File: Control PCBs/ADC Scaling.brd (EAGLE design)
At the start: 50 x 50 mm, 25 parts, among them K1 G5V-2, K2 G5V-2, K3 G5V-2, K4 G5V-2

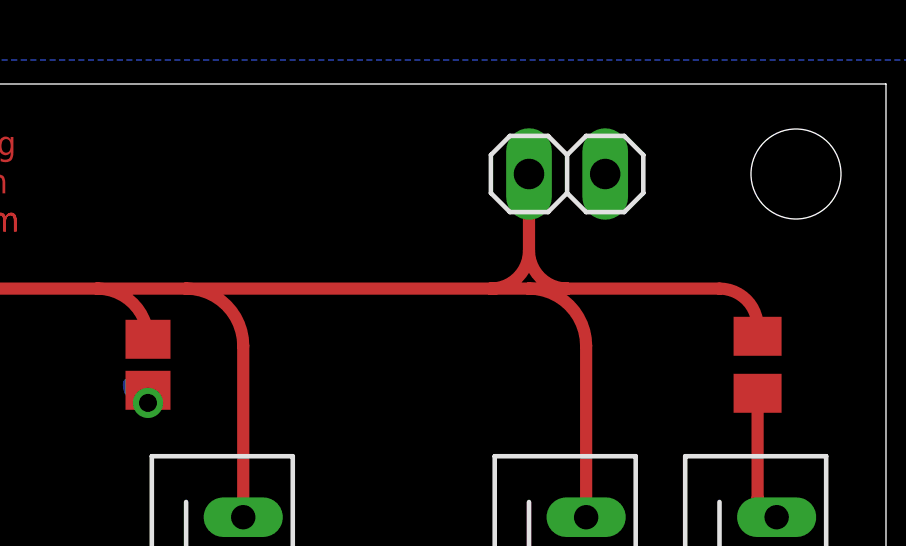
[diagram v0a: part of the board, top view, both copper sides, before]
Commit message: +Flip out connector on scaling pcb to aid in routing the adc +Routed ADC part of ADC/DAC board
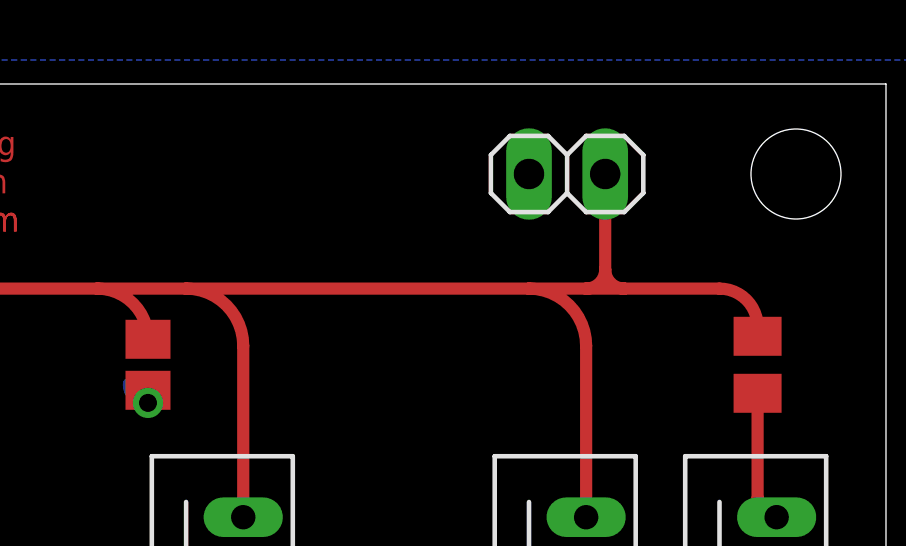
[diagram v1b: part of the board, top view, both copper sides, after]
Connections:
- net GND: now also JP2.1; no longer JP2.2
- net N$21: now also JP2.2; no longer JP2.1
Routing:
- net N$21: track 82.8 -> 81.6 mm
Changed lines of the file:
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@@
 <contactref element="R3" pad="S"/>
 <contactref element="R3" pad="A"/>
-<contactref element="JP2" pad="2"/>
 <contactref element="K1" pad="13"/>
 <contactref element="K1" pad="4"/>
@@
 <wire x1="7.62" y1="39.155" x2="5.295" y2="39.155" width="0.4064" layer="1"/>
 <wire x1="5.295" y1="39.155" x2="3.81" y2="40.64" width="0.4064" layer="1" curve="-90"/>
+<contactref element="JP2" pad="1"/>
 </signal>
 <signal name="N$1">
@@
 </signal>
 <signal name="N$21">
-<contactref element="JP2" pad="1"/>
 <contactref element="R7" pad="E"/>
 <contactref element="R4" pad="E"/>
@@
 <wire x1="15.24" y1="43.18" x2="23.71" y2="43.18" width="0.4064" layer="1"/>
 <wire x1="23.71" y1="43.18" x2="26.67" y2="43.18" width="0.4064" layer="1"/>
-<wire x1="26.67" y1="43.18" x2="36.83" y2="43.18" width="0.4064" layer="1"/>
-<wire x1="36.83" y1="43.18" x2="38.1" y2="43.18" width="0.4064" layer="1"/>
-<wire x1="38.1" y1="43.18" x2="39.37" y2="43.18" width="0.4064" layer="1"/>
-<wire x1="39.37" y1="43.18" x2="44.45" y2="43.18" width="0.4064" layer="1"/>
+<wire x1="26.67" y1="43.18" x2="38.1" y2="43.18" width="0.4064" layer="1"/>
+<wire x1="38.1" y1="43.18" x2="40.005" y2="43.18" width="0.4064" layer="1"/>
+<wire x1="40.005" y1="43.18" x2="41.275" y2="43.18" width="0.4064" layer="1"/>
+<wire x1="41.275" y1="43.18" x2="44.45" y2="43.18" width="0.4064" layer="1"/>
 <wire x1="44.45" y1="43.18" x2="45.72" y2="41.91" width="0.4064" layer="1" curve="-90"/>
 <wire x1="45.72" y1="41.91" x2="45.72" y2="41.59" width="0.4064" layer="1"/>
@@
 <contactref element="C1" pad="1"/>
 <wire x1="25.4" y1="41.49" x2="23.71" y2="43.18" width="0.4064" layer="1" curve="90"/>
-<wire x1="38.1" y1="44.45" x2="36.83" y2="43.18" width="0.4064" layer="1" curve="-90"/>
-<wire x1="38.1" y1="47" x2="38.1" y2="44.45" width="0.4064" layer="1"/>
-<wire x1="38.1" y1="44.45" x2="39.37" y2="43.18" width="0.4064" layer="1" curve="90"/>
+<contactref element="JP2" pad="2"/>
+<wire x1="40.64" y1="43.815" x2="40.005" y2="43.18" width="0.4064" layer="1" curve="-90"/>
+<wire x1="40.64" y1="47" x2="40.64" y2="43.815" width="0.4064" layer="1"/>
+<wire x1="40.64" y1="43.815" x2="41.275" y2="43.18" width="0.4064" layer="1" curve="90"/>
 </signal>
 <signal name="N$22">
